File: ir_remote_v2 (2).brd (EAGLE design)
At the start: 100 x 80 mm, 25 parts, among them IC1 AP1117E50G, Q5 10MHz, T11 TASTER3301, T12 TASTER3301, T13 TASTER3301, T14 TASTER3301, T15 TASTER3301

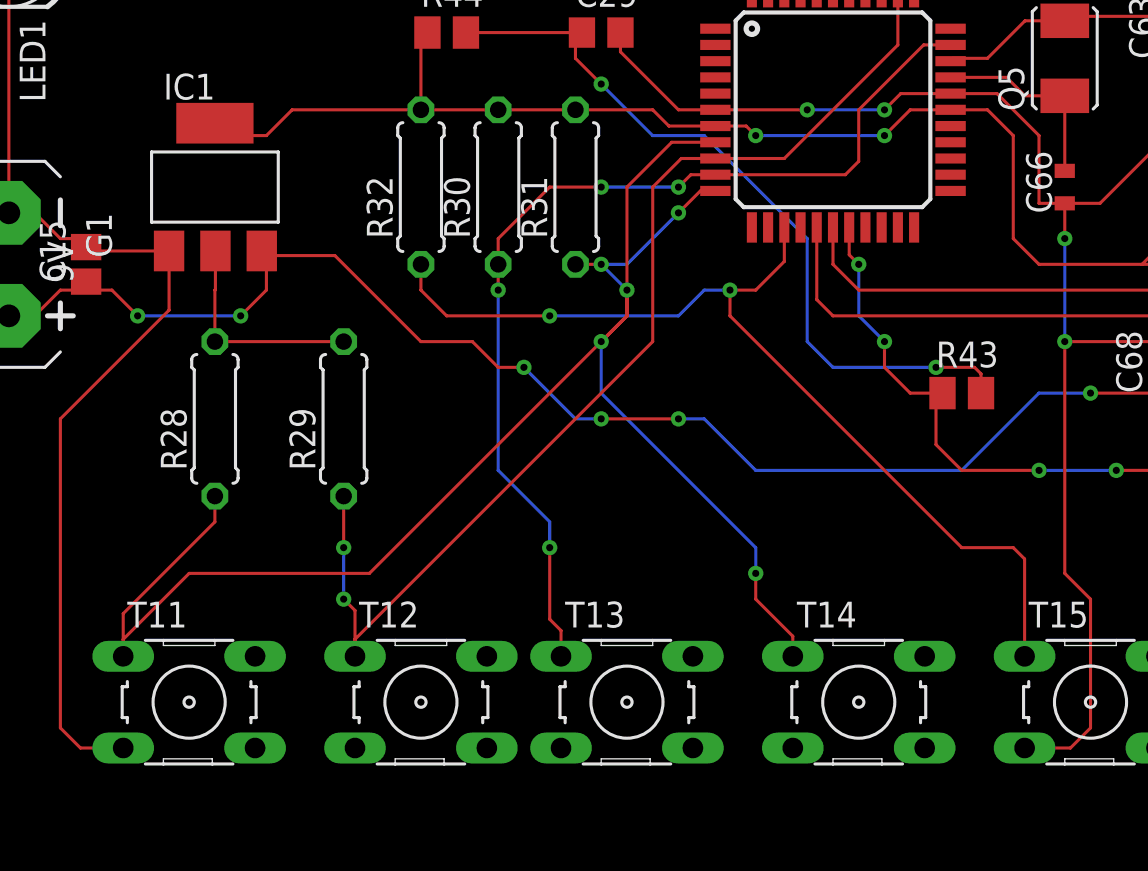
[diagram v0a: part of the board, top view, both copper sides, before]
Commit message: Add files via upload
PCB Layout - Fixed Design Rules, no recommendation from Volpe/Wegmann
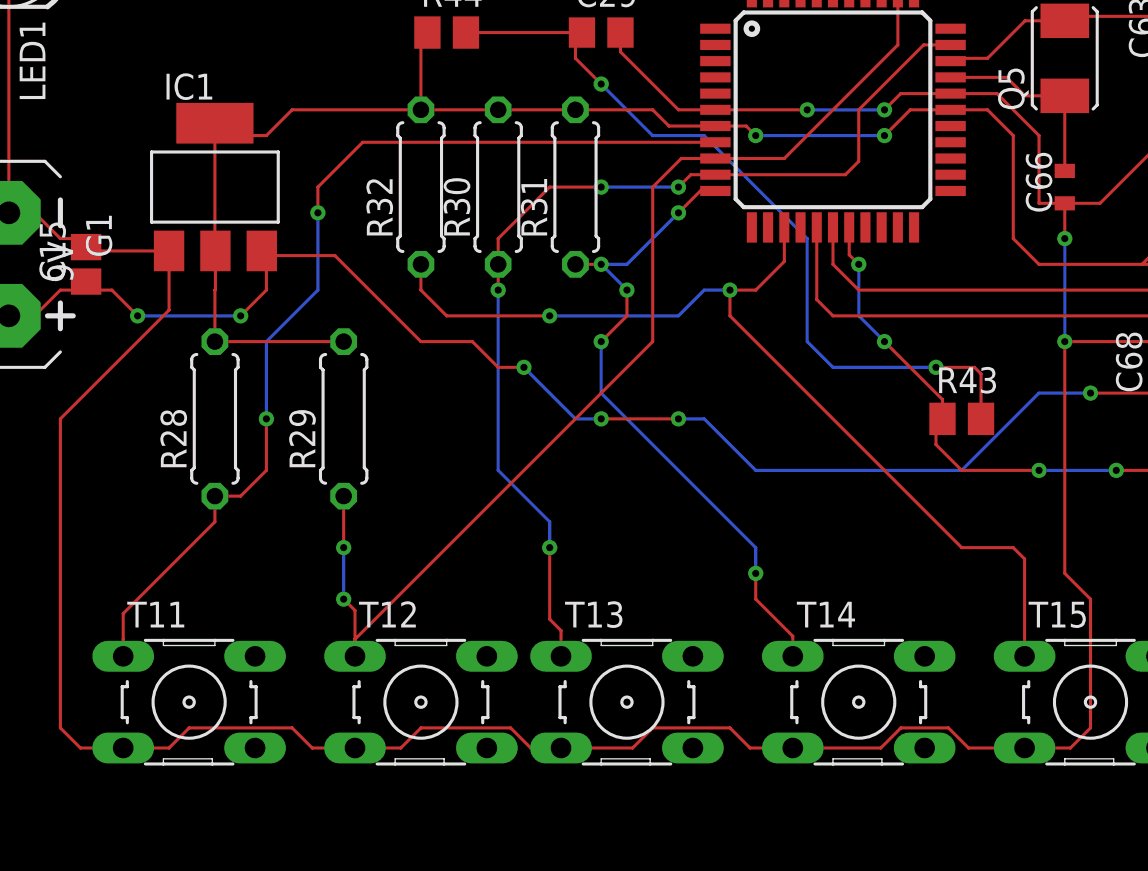
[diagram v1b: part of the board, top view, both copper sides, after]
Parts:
- moved R43 1.27 mm to (50.8, 24.1)
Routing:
- net GND: track 163.9 -> 212.4 mm
- net VCC: track 105.4 -> 111.7 mm
- net RB0: track 53.7 -> 49.2 mm, vias 0 -> 2
- net N$24: track 37.5 -> 38.8 mm
- net MCLR: track 48.8 -> 47.8 mm
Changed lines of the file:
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@@
 <attribute name="VALUE" x="41.6306" y="50.165" size="1.27" layer="27" ratio="10" rot="R180"/>
 </element>
-<element name="R43" library="rcl" package="M0805" value="470" x="50.8" y="25.4" smashed="yes">
-<attribute name="NAME" x="49.53" y="26.67" size="1.27" layer="25"/>
-<attribute name="VALUE" x="49.53" y="22.86" size="1.27" layer="27"/>
+<element name="R43" library="rcl" package="M0805" value="470" x="50.8" y="24.13" smashed="yes">
+<attribute name="NAME" x="49.53" y="25.4" size="1.27" layer="25"/>
+<attribute name="VALUE" x="49.53" y="21.59" size="1.27" layer="27"/>
 </element>
 <element name="R44" library="rcl" package="M0805" value="10k" x="25.4" y="43.18" smashed="yes">
@@
 <wire x1="60.64" y1="27.94" x2="60.96" y2="27.62" width="0.1524" layer="1"/>
 <wire x1="3.81" y1="45.72" x2="3.81" y2="34.29" width="0.1524" layer="1"/>
-<wire x1="42.4688" y1="7.8994" x2="53.8988" y2="7.8994" width="0" layer="19" extent="1-1"/>
-<wire x1="31.0388" y1="7.8994" x2="42.4688" y2="7.8994" width="0" layer="19" extent="1-1"/>
-<wire x1="20.8788" y1="7.8994" x2="31.0388" y2="7.8994" width="0" layer="19" extent="1-1"/>
-<wire x1="9.4488" y1="7.8994" x2="20.8788" y2="7.8994" width="0" layer="19" extent="1-1"/>
+<wire x1="42.4688" y1="7.8994" x2="46.808275" y2="7.8994" width="0.1524" layer="1"/>
+<wire x1="47.798875" y1="8.89" x2="46.808275" y2="7.8994" width="0.1524" layer="1"/>
+<wire x1="53.8988" y1="7.8994" x2="51.134125" y2="7.8994" width="0.1524" layer="1"/>
+<wire x1="51.134125" y1="7.8994" x2="50.143525" y2="8.89" width="0.1524" layer="1"/>
+<wire x1="50.143525" y1="8.89" x2="47.798875" y2="8.89" width="0.1524" layer="1"/>
+<wire x1="42.4688" y1="7.8994" x2="40.3606" y2="7.8994" width="0.1524" layer="1"/>
+<wire x1="40.3606" y1="7.8994" x2="39.37" y2="8.89" width="0.1524" layer="1"/>
+<wire x1="35.56" y1="8.89" x2="39.37" y2="8.89" width="0.1524" layer="1"/>
+<wire x1="31.0388" y1="7.8994" x2="34.5694" y2="7.8994" width="0.1524" layer="1"/>
+<wire x1="34.5694" y1="7.8994" x2="35.56" y2="8.89" width="0.1524" layer="1"/>
+<wire x1="30.2006" y1="7.8994" x2="31.0388" y2="7.8994" width="0.1524" layer="1"/>
+<wire x1="24.13" y1="8.89" x2="23.1394" y2="7.8994" width="0.1524" layer="1"/>
+<wire x1="28.553525" y1="8.89" x2="24.13" y2="8.89" width="0.1524" layer="1"/>
+<wire x1="31.0388" y1="7.8994" x2="29.544125" y2="7.8994" width="0.1524" layer="1"/>
+<wire x1="29.544125" y1="7.8994" x2="28.553525" y2="8.89" width="0.1524" layer="1"/>
+<wire x1="9.4488" y1="7.8994" x2="11.7094" y2="7.8994" width="0.1524" layer="1"/>
+<wire x1="11.7094" y1="7.8994" x2="12.7" y2="8.89" width="0.1524" layer="1"/>
+<wire x1="17.78" y1="8.89" x2="12.7" y2="8.89" width="0.1524" layer="1"/>
+<wire x1="23.1394" y1="7.8994" x2="20.8788" y2="7.8994" width="0.1524" layer="1"/>
+<wire x1="20.8788" y1="7.8994" x2="18.7706" y2="7.8994" width="0.1524" layer="1"/>
+<wire x1="18.7706" y1="7.8994" x2="17.78" y2="8.89" width="0.1524" layer="1"/>
 </signal>
 <signal name="VCC">
@@
 <wire x1="24.45" y1="43.18" x2="24.13" y2="42.86" width="0.1524" layer="1"/>
 <wire x1="24.13" y1="42.86" x2="24.13" y2="39.37" width="0.1524" layer="1"/>
-<wire x1="13.9954" y1="32.4104" x2="13.97" y2="38.7096" width="0" layer="19" extent="1-1"/>
+<wire x1="13.9954" y1="32.4104" x2="13.97" y2="32.4358" width="0.1524" layer="1"/>
+<wire x1="13.97" y1="32.4358" x2="13.97" y2="38.7096" width="0.1524" layer="1"/>
 </signal>
 <signal name="D0_LCD">
@@
 <wire x1="46.99" y1="27.94" x2="45.72" y2="29.21" width="0.1524" layer="16"/>
 <via x="46.99" y="27.94" extent="1-16" drill="0.35"/>
-<wire x1="49.85" y1="25.4" x2="48.26" y2="25.4" width="0.1524" layer="1"/>
-<wire x1="48.26" y1="25.4" x2="46.99" y2="26.67" width="0.1524" layer="1"/>
-<wire x1="46.99" y1="26.67" x2="46.99" y2="27.94" width="0.1524" layer="1"/>
+<wire x1="49.85" y1="24.13" x2="49.85" y2="25.08" width="0.1524" layer="1"/>
+<wire x1="49.85" y1="25.08" x2="46.99" y2="27.94" width="0.1524" layer="1"/>
 <wire x1="45.72" y1="29.21" x2="45.72" y2="31.75" width="0.1524" layer="16"/>
-<wire x1="49.85" y1="25.4" x2="49.53" y2="25.08" width="0.1524" layer="1"/>
-<wire x1="49.53" y1="25.08" x2="49.53" y2="22.86" width="0.1524" layer="1"/>
+<wire x1="49.85" y1="24.13" x2="49.53" y2="23.81" width="0.1524" layer="1"/>
+<wire x1="49.53" y1="23.81" x2="49.53" y2="22.86" width="0.1524" layer="1"/>
 <wire x1="49.53" y1="22.86" x2="50.8" y2="21.59" width="0.1524" layer="1"/>
 <wire x1="50.8" y1="21.59" x2="54.61" y2="21.59" width="0.1524" layer="1"/>
@@
 <wire x1="44.45" y1="26.67" x2="49.53" y2="26.67" width="0.1524" layer="16"/>
 <via x="49.53" y="26.67" extent="1-16" drill="0.35"/>
-<wire x1="51.75" y1="25.4" x2="51.75" y2="26.35" width="0.1524" layer="1"/>
+<wire x1="51.75" y1="24.13" x2="51.75" y2="26.35" width="0.1524" layer="1"/>
 <wire x1="51.75" y1="26.35" x2="51.43" y2="26.67" width="0.1524" layer="1"/>
 <wire x1="51.43" y1="26.67" x2="49.53" y2="26.67" width="0.1524" layer="1"/>
@@
 <contactref element="T11" pad="1"/>
 <contactref element="R28" pad="1"/>
-<wire x1="38.65" y1="37.77" x2="36.5" y2="37.77" width="0.1524" layer="1"/>
-<wire x1="36.5" y1="37.77" x2="34.29" y2="35.56" width="0.1524" layer="1"/>
-<wire x1="21.59" y1="16.51" x2="12.7" y2="16.51" width="0.1524" layer="1"/>
 <wire x1="9.4488" y1="13.2588" x2="9.4488" y2="12.4206" width="0.1524" layer="1"/>
-<wire x1="34.29" y1="35.56" x2="34.29" y2="29.21" width="0.1524" layer="1"/>
-<wire x1="34.29" y1="29.21" x2="21.59" y2="16.51" width="0.1524" layer="1"/>
-<wire x1="12.7" y1="16.51" x2="9.4488" y2="13.2588" width="0.1524" layer="1"/>
 <wire x1="13.97" y1="20.32" x2="13.97" y2="19.05" width="0.1524" layer="1"/>
 <wire x1="9.4488" y1="14.5288" x2="9.4488" y2="12.4206" width="0.1524" layer="1"/>
 <wire x1="13.97" y1="19.05" x2="9.4488" y2="14.5288" width="0.1524" layer="1"/>
+<wire x1="38.65" y1="37.77" x2="21.26" y2="37.77" width="0.1524" layer="1"/>
+<wire x1="21.26" y1="37.77" x2="19.05" y2="35.56" width="0.1524" layer="1"/>
+<wire x1="19.05" y1="35.56" x2="19.05" y2="34.29" width="0.1524" layer="1"/>
+<via x="19.05" y="34.29" extent="1-16" drill="0.35"/>
+<wire x1="19.05" y1="34.29" x2="19.05" y2="30.48" width="0.1524" layer="16"/>
+<wire x1="19.05" y1="30.48" x2="16.51" y2="27.94" width="0.1524" layer="16"/>
+<wire x1="16.51" y1="27.94" x2="16.51" y2="24.13" width="0.1524" layer="16"/>
+<via x="16.51" y="24.13" extent="1-16" drill="0.35"/>
+<wire x1="16.51" y1="21.59" x2="15.24" y2="20.32" width="0.1524" layer="1"/>
+<wire x1="15.24" y1="20.32" x2="13.97" y2="20.32" width="0.1524" layer="1"/>
+<wire x1="16.51" y1="24.13" x2="16.51" y2="21.59" width="0.1524" layer="1"/>
 </signal>
 <signal name="RD0_LED">
